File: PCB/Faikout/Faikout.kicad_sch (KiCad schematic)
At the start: 47 parts, among them J1 1x5, J2 TC2030-USB-NL, J3 Reset, Q1 BSS138PS, U1 TPS562246, U4 ESP32-S3-MINI-1

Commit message: KiCAD 10
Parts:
- D2, D3, V1, V2, V3, V4, V5, V6: value ~ -> (none)

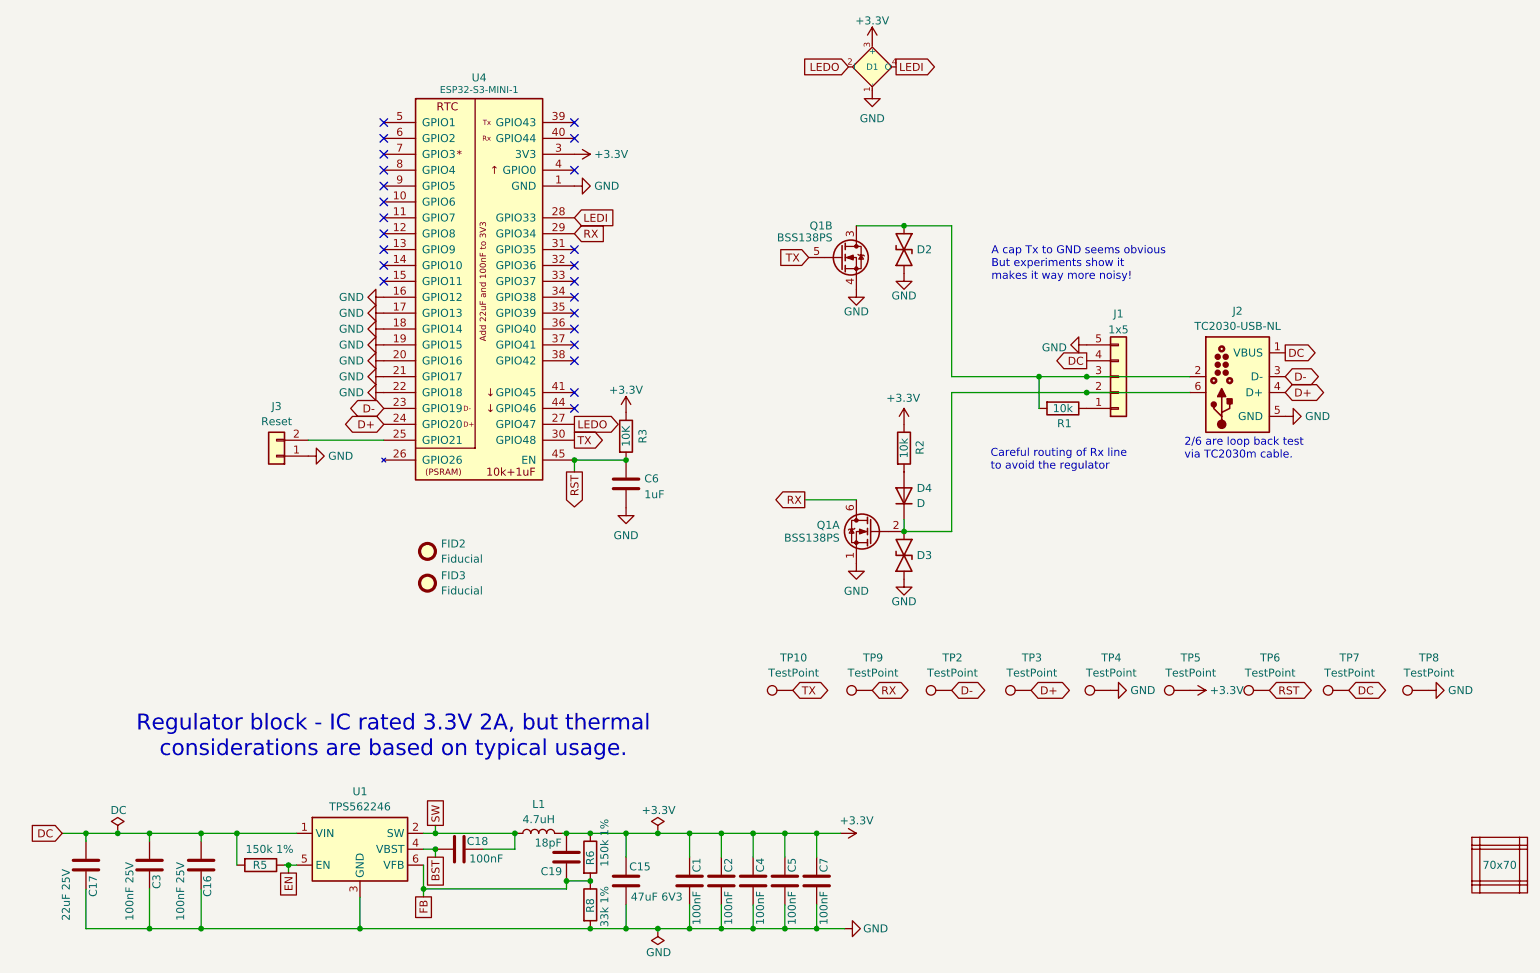
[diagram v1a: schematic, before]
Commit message: Label max voltage
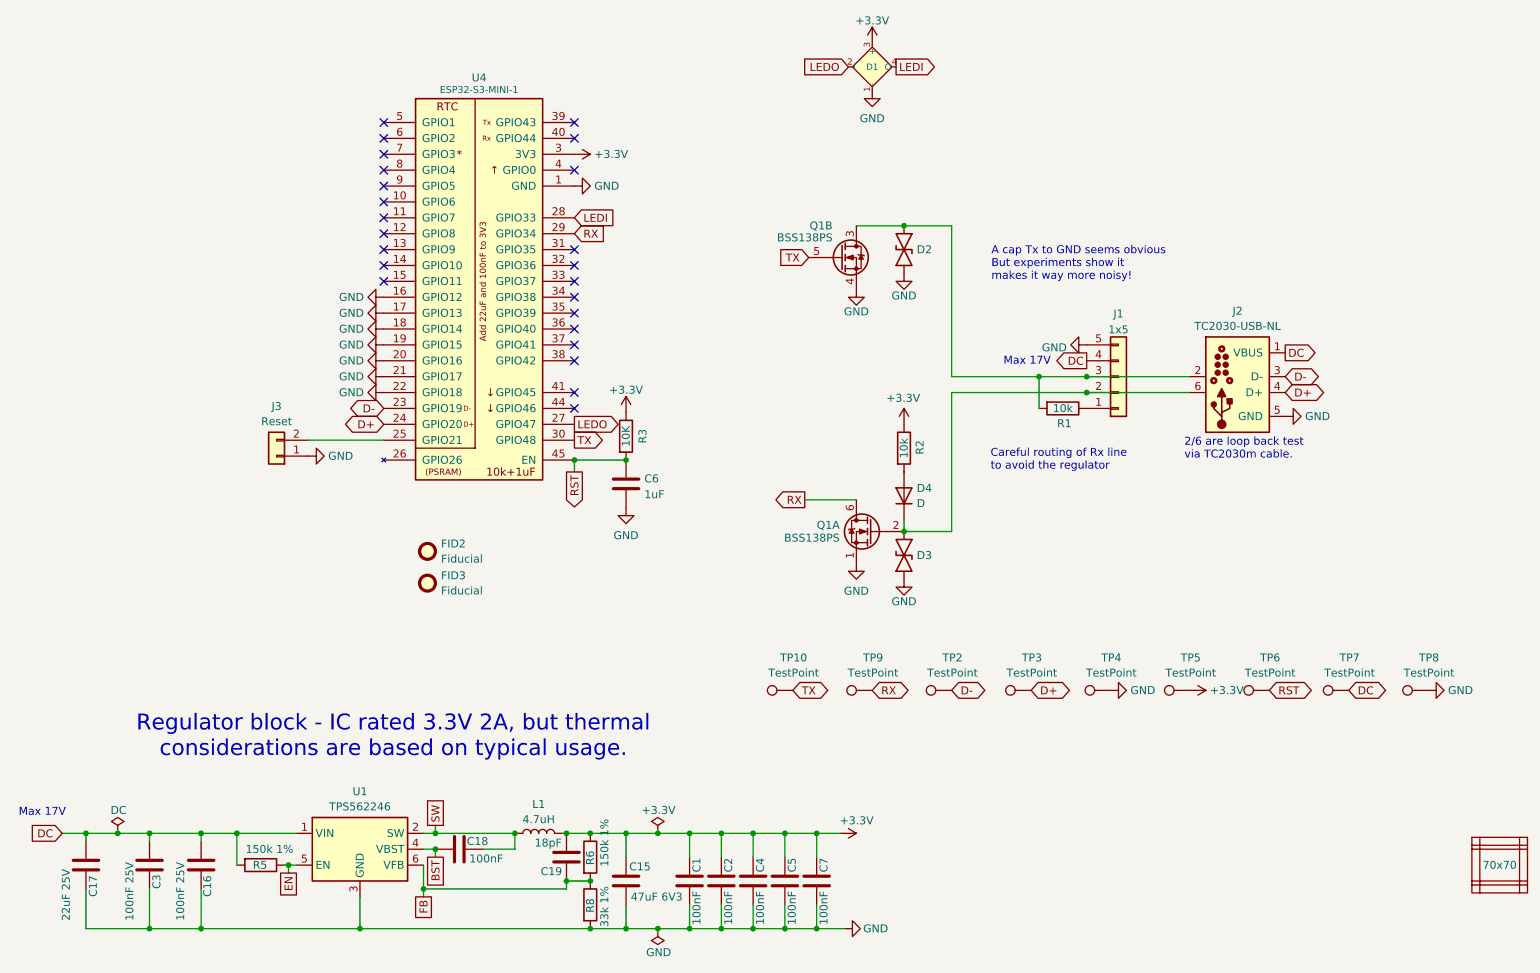
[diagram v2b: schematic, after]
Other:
- note added: "Max 17V"
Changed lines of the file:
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@@
 		(comment 2 "www.me.uk")
+	)
+	(text "Max 17V"
+		(exclude_from_sim no)
+		(at 29.21 165.608 0)
+		(effects
+			(font
+				(size 1.27 1.27)
+			)
+		)
 	)
 	(text "Careful routing of Rx line\nto avoid the regulator"
@@
 		)
 	)
+	(text "Max 17V"
+		(exclude_from_sim no)
+		(at 186.69 93.472 0)
+		(effects
+			(font
+				(size 1.27 1.27)
+			)
+		)
+	)

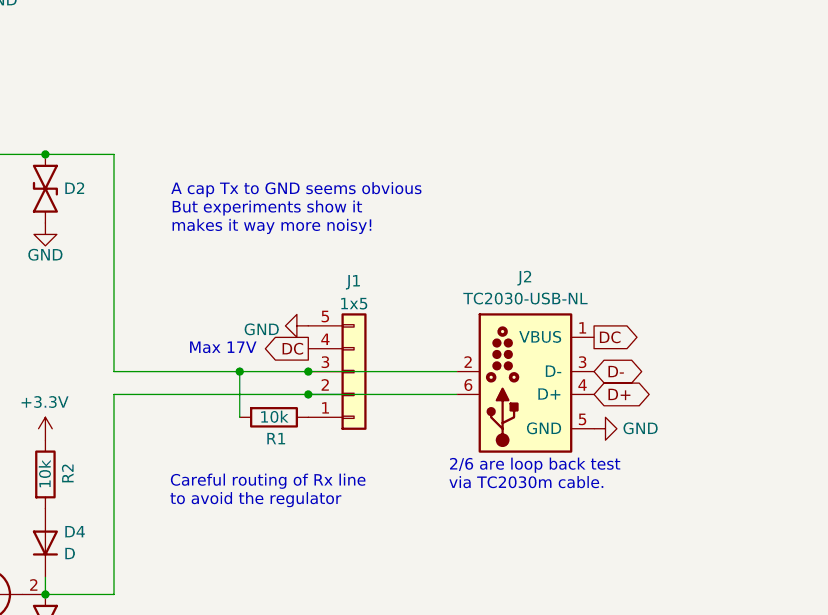
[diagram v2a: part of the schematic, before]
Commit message: Remove logos & update the PCB to use 1x6 header instead of TC2030
Transitioned the programming interface to a more standard pin header and removed branding elements to make the project more open-source friendly.
* Programming Header (J2):
    * Replaced the TC2030 (Tag-Connect) interface with a standard 1x06 2.54mm vertical pin header.
    * Updated the footprint to Connector_PinHeader_2.54mm:PinHeader_1x06_P2.54mm_Vertical.
    * Updated schematic symbols and adjusted routing for the new header pinout (D+, D-, DC, and GND).
    * Updated schematic annotations to refer to "programming cable" instead of "TC2030m".
* Logo & Branding Removal:
    * Deleted "Andrews & Arnold Ltd" branding and AJK logos from the silkscreen.
    * Removed text elements referencing the original manufacturer (e.g., "Designed by RevK", "Made in China for...").
    * Updated project metadata (company name) to "Open Source".
* Misc Improvements:
    * Reoriented global labels and power symbols for better schematic readability.
    * Synchronized KiCad project files and updated footprint cache.
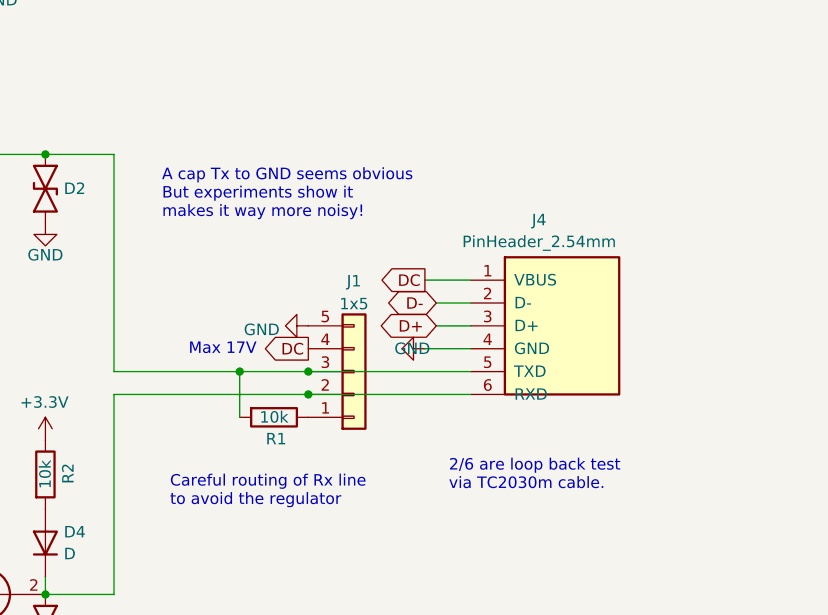
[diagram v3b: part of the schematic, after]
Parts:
- removed J2: TC2030-USB-NL, RevK:Tag-Connect_TC2030-IDC-NL_2x03_P1.27mm_Vertical, symbol RevK:TC2030-USB-NL-LB
- added J4: PinHeader_2.54mm, Connector_PinHeader_2.54mm:PinHeader_1x06_P2.54mm_Vertical, symbol Faikin:Conn_01x06_Programming
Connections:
- net D+: now also J4.3 (D+)
- net D-: now also J4.2 (D-)
- net DC: now also J4.1 (VBUS)
- net GND: now also J4.4 (GND)
- net at D3.2, D4.1 (K), J1.2 (Pin_2)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: now also J4.6 (RXD)
- net at D2.2, J1.3 (Pin_3), Q1.3 (SP)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: now also J4.5 (TXD)
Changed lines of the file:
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@@
 	(text "A cap Tx to GND seems obvious\nBut experiments show it\nmakes it way more noisy!"
 		(exclude_from_sim no)
-		(at 180.975 80.645 0)
+		(at 179.959 78.994 0)
 		(effects
 			(font
@@
 	(wire
 		(pts
-			(xy 196.215 98.425) (xy 212.725 98.425)
+			(xy 196.215 98.425) (xy 214.249 98.425)
 		)
 		(stroke
@@
 	(wire
 		(pts
+			(xy 210.439 88.265) (xy 214.249 88.265)
+		)
+		(stroke
+			(width 0)
+			(type default)
+		)
+	)
+	(wire
+		(pts
 			(xy 90.17 177.8) (xy 90.17 179.07)
 		)
@@
 	(wire
 		(pts
+			(xy 209.169 93.345) (xy 214.249 93.345)
+		)
+		(stroke
+			(width 0)
+			(type default)
+		)
+	)
+	(wire
+		(pts
 			(xy 116.84 168.91) (xy 122.555 168.91)
 		)
@@
 	(wire
 		(pts
+			(xy 209.169 85.725) (xy 214.249 85.725)
+		)
+		(stroke
+			(width 0)
+			(type default)
+		)
+	)
+	(wire
+		(pts
 			(xy 80.01 184.15) (xy 80.01 179.07)
 		)
@@
 	(wire
 		(pts
-			(xy 196.215 95.885) (xy 212.725 95.885)
+			(xy 196.215 95.885) (xy 214.249 95.885)
 		)
 		(stroke
@@
 	(wire
 		(pts
+			(xy 210.439 90.805) (xy 214.249 90.805)
+		)
+		(stroke
+			(width 0)
+			(type default)
+		)
+	)
+	(wire
+		(pts
 			(xy 127.635 168.91) (xy 132.715 168.91)
 		)
@@
 	(global_label "D-"
 		(shape bidirectional)
-		(at 227.965 95.885 0)
+		(at 210.439 88.265 180)
 		(fields_autoplaced yes)
 		(effects
@@
 				(size 1.27 1.27)
 			)
-			(justify left)
+			(justify right)
 		)
 		(property "Intersheetrefs" "${INTERSHEET_REFS}"
-			(at 234.0909 95.885 0)
+			(at 204.3131 88.265 0)
 			(hide yes)
 			(show_name no)
@@
 					(size 1.27 1.27)
 				)
-				(justify left)
+				(justify right)
 			)
 		)
@@
 	(global_label "D+"
 		(shape bidirectional)
-		(at 227.965 98.425 0)
+		(at 210.439 90.805 180)
 		(fields_autoplaced yes)
 		(effects
@@
 				(size 1.27 1.27)
 			)
-			(justify left)
+			(justify right)
 		)
 		(property "Intersheetrefs" "${INTERSHEET_REFS}"
-			(at 234.0909 98.425 0)
+			(at 204.3131 90.805 0)
 			(hide yes)
 			(show_name no)
@@
 					(size 1.27 1.27)
 				)
-				(justify left)
+				(justify right)
 			)
 		)
@@
 	(global_label "DC"
 		(shape output)
-		(at 227.965 92.075 0)
+		(at 209.169 85.725 180)
 		(fields_autoplaced yes)
 		(effects
@@
 				(size 1.27 1.27)
 			)
-			(justify left)
+			(justify right)
 		)
 		(property "Intersheetrefs" "${INTERSHEET_REFS}"
-			(at 232.836 92.075 0)
+			(at 204.298 85.725 0)
 			(hide yes)
 			(show_name no)
@@
 					(size 1.27 1.27)
 				)
-				(justify left)
+				(justify right)
 			)
 		)
@@
 	)
 	(symbol
-		(lib_id "RevK:TC2030-USB-NL-LB")
-		(at 220.345 97.155 0)
-		(unit 1)
-		(body_style 1)
-		(exclude_from_sim no)
-		(in_bom no)
-		(on_board yes)
-		(in_pos_files yes)
-		(dnp no)
-		(fields_autoplaced yes)
-		(property "Reference" "J2"
-			(at 220.345 85.3905 0)
-			(show_name no)
-			(do_not_autoplace no)
-			(effects
-				(font
-					(size 1.27 1.27)
-				)
-			)
-		)
-		(property "Value" "TC2030-USB-NL"
-			(at 220.345 87.8148 0)
-			(show_name no)
-			(do_not_autoplace no)
-			(effects
-				(font
-					(size 1.27 1.27)
-				)
-			)
-		)
-		(property "Footprint" "RevK:Tag-Connect_TC2030-IDC-NL_2x03_P1.27mm_Vertical"
-			(at 220.091 106.299 0)
-			(hide yes)
-			(show_name no)
-			(do_not_autoplace no)
-			(effects
-				(font
-					(size 1.27 1.27)
-				)
-			)
-		)
-		(property "Datasheet" ""
-			(at 224.155 98.425 0)
-			(hide yes)
-			(show_name no)
-			(do_not_autoplace no)
-			(effects
-				(font
-					(size 1.27 1.27)
-				)
-			)
-		)
-		(property "Description" "TC2030-USB-NL"
-			(at 220.345 84.455 0)
-			(hide yes)
-			(show_name no)
-			(do_not_autoplace no)
-			(effects
-				(font
-					(size 1.27 1.27)
-				)
-			)
-		)
-		(pin "5"
-		)
-		(pin "6"
-		)
-		(pin "1"
-		)
-		(pin "4"
-		)
-		(pin "3"
-		)
-		(pin "2"
-		)
-		(instances
-			(project "Faikout"
-				(path "/46c350bb-7de4-4e81-aafd-4af55e37aab0"
-					(reference "J2")
-					(unit 1)
-				)
-			)
-		)
-	)
-	(symbol
 		(lib_id "power:GND")
 		(at 114.3 65.405 90)
@@
 	(symbol
 		(lib_id "power:GND")
-		(at 227.965 102.235 90)
+		(at 209.169 93.345 270)
 		(unit 1)
 		(body_style 1)
@@
 		(in_pos_files yes)
 		(dnp no)
-		(fields_autoplaced yes)
 		(property "Reference" "#PWR016"
-			(at 234.315 102.235 0)
+			(at 202.819 93.345 0)
 			(hide yes)
 			(show_name no)
@@
 		)
 		(property "Value" "GND"
-			(at 231.14 102.235 90)
+			(at 207.772 93.345 90)
 			(show_name no)
 			(do_not_autoplace no)
@@
 					(size 1.27 1.27)
 				)
-				(justify right)
 			)
 		)
 		(property "Footprint" ""
-			(at 227.965 102.235 0)
+			(at 209.169 93.345 0)
 			(hide yes)
 			(show_name no)
@@
 		)
 		(property "Datasheet" ""
-			(at 227.965 102.235 0)
+			(at 209.169 93.345 0)
 			(hide yes)
 			(show_name no)
@@
 		)
 		(property "Description" "Power symbol creates a global label with name \"GND\" , ground"
-			(at 227.965 102.235 0)
+			(at 209.169 93.345 0)
 			(hide yes)
 			(show_name no)
@@
 					(unit 1)
 				)
+			)
+		)
+	)
+	(symbol
+		(lib_id "Faikin:Conn_01x06_Programming")
+		(at 221.869 90.805 0)
+		(unit 1)
+		(body_style 1)
+		(exclude_from_sim no)
+		(in_bom no)
+		(on_board yes)
+		(in_pos_files yes)
+		(dnp no)
+		(fields_autoplaced yes)
+		(property "Reference" "J4"
+			(at 221.869 79.0405 0)
+			(show_name no)
+			(do_not_autoplace no)
+			(effects
+				(font
+					(size 1.27 1.27)
+				)
+			)
+		)
+		(property "Value" "PinHeader_2.54mm"
+			(at 221.869 81.4648 0)
+			(show_name no)
+			(do_not_autoplace no)
+			(effects
+				(font
+					(size 1.27 1.27)
+				)
+			)
+		)
+		(property "Footprint" "Connector_PinHeader_2.54mm:PinHeader_1x06_P2.54mm_Vertical"
+			(at 221.615 99.949 0)
+			(hide yes)
+			(show_name no)
+			(do_not_autoplace no)
+			(effects
+				(font
+					(size 1.27 1.27)
+				)
+			)
+		)
+		(property "Datasheet" ""
+			(at 225.679 92.075 0)
+			(hide yes)
+			(show_name no)
+			(do_not_autoplace no)
+			(effects
+				(font
+					(size 1.27 1.27)
+				)
+			)
+		)
+		(property "Description" "PinHeader_2.54mm"
+			(at 221.869 78.105 0)
+			(hide yes)
+			(show_name no)
+			(do_not_autoplace no)
+			(effects
+				(font
+					(size 1.27 1.27)
+				)
+			)
+		)
+		(pin "5"
+		)
+		(pin "6"
+		)
+		(pin "1"
+		)
+		(pin "4"
+		)
+		(pin "3"
+		)
+		(pin "2"
+		)
+		(instances
+			(project "Faikout"
+				(path "/46c350bb-7de4-4e81-aafd-4af55e37aab0"
+					(reference "J4")
+					(unit 1)
+				)
